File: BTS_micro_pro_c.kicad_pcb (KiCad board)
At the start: 2 copper layers, 33 x 17.8 mm, 5 parts, among them J1 FTDI, J2 I2C, J3 Analog, J6 Analog, J7 Digital

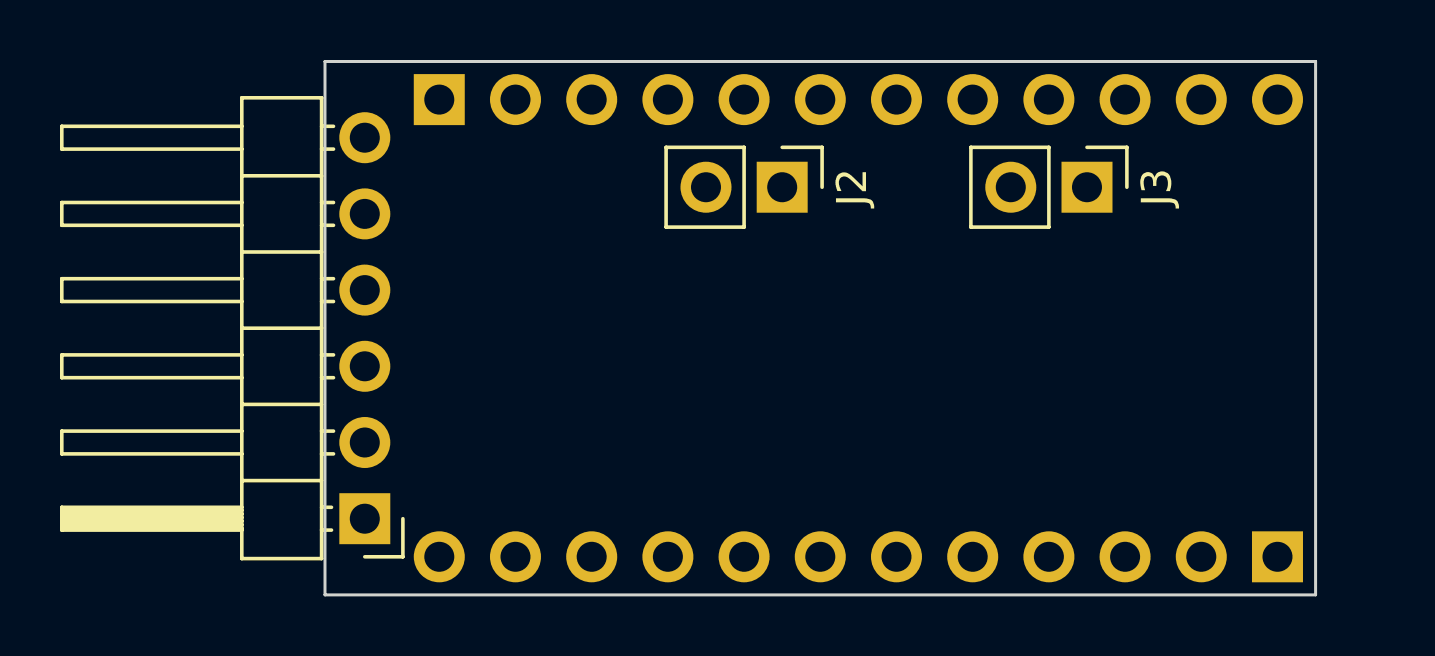
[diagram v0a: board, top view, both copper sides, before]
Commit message: Schematic potentially done, needs footprints assigned though.
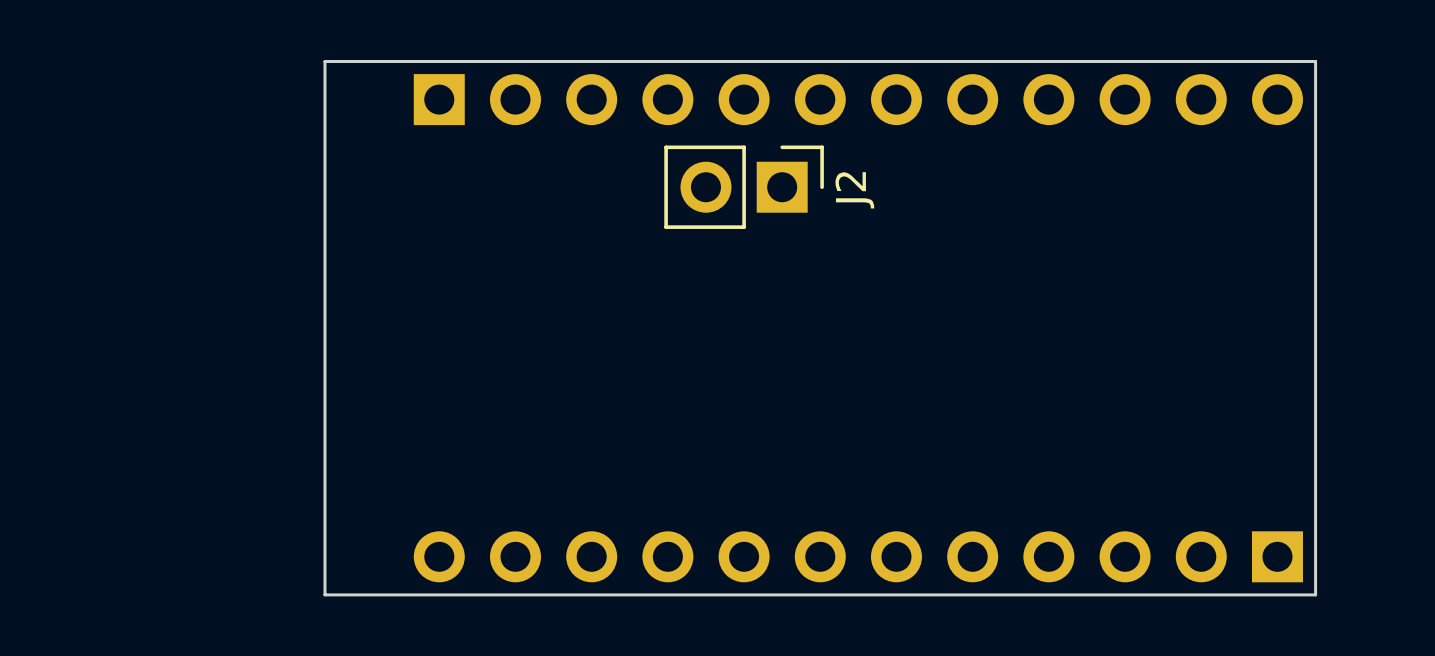
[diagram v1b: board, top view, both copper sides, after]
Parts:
- removed J1: FTDI, Connector_PinHeader_2.54mm:PinHeader_1x06_P2.54mm_Horizontal
- removed J3: Analog, Connector_PinHeader_2.54mm:PinHeader_1x02_P2.54mm_Vertical

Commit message: Finish rev1.
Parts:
- removed J2: I2C, Connector_PinHeader_2.54mm:PinHeader_1x02_P2.54mm_Vertical
- added C1: 10uF, Capacitor_SMD:C_0402_1005Metric, F.Cu at (114.1, 88.0)
- added C2: 22uF, Capacitor_SMD:C_0402_1005Metric, F.Cu at (114.9, 90.1)
- added C3: 22pF, Capacitor_SMD:C_0402_1005Metric, F.Cu at (128.8, 93.0)
- added C4: 22pF, Capacitor_SMD:C_0402_1005Metric, F.Cu at (128.9, 96.0)
- added C5: 1uF, Capacitor_SMD:C_0402_1005Metric, F.Cu at (116.5, 95.0)
- added C6: 0.1uF, Capacitor_SMD:C_0402_1005Metric, F.Cu at (116.1, 89.0)
- added C7: 1uF, Capacitor_SMD:C_0402_1005Metric, F.Cu at (114.1, 87.0)
- added C8: 0.1uF, Capacitor_SMD:C_0402_1005Metric, F.Cu at (114.1, 86.1)
- added D1: LED, LED_SMD:LED_0402_1005Metric, F.Cu at (130.7, 86.2)
- added D2: D, Diode_SMD:D_0402_1005Metric, F.Cu at (113.0, 90.9)
- added F1: 500mA Polyfuse, Fuse:Fuse_0805_2012Metric, F.Cu at (111.2, 91.1)
- added J1: USB4105-GF-A, USB4105-GF-A:GCT_USB4105-GF-A, F.Cu at (102.9, 91.1)
- added R1: 330, Resistor_SMD:R_0402_1005Metric, F.Cu at (128.8, 86.2)
- added R2: 1M, Resistor_SMD:R_0402_1005Metric, F.Cu at (128.4, 94.5)
- added R3: 10K, Resistor_SMD:R_0402_1005Metric, F.Cu at (123.4, 96.4)
- added R6: 5.1k, Resistor_SMD:R_0402_1005Metric, F.Cu at (109.0, 89.4)
- added R7: 5.1k, Resistor_SMD:R_0402_1005Metric, F.Cu at (109.0, 93.7)
- added R8: 10k, Resistor_SMD:R_0402_1005Metric, F.Cu at (122.9, 85.3)
- added U1: ATmega32U4-A, Package_DFN_QFN:QFN-44-1EP_7x7mm_P0.5mm_EP5.2x5.2mm, F.Cu at (121.2, 91.2)
- added U3: AMS1117-3.3, Package_TO_SOT_SMD:SOT-23-3, F.Cu at (111.2, 87.3)
- added Y1: 8Mhz Crystal, Crystal:Crystal_SMD_3225-4Pin_3.2x2.5mm, F.Cu at (131.1, 93.8)
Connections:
- net /~{RESET} renamed ~{RESET}
- J6 pad 1: VDC -> UVCC
- J6 pad 10: /MISO/D12 -> MISO/D12
- J6 pad 11: /MOSI/*D11 -> MOSI/*D11
- J6 pad 12: /SS/*D10 -> SS/*D10
- J6 pad 5: /A3 -> A3
- J6 pad 6: /A2 -> A2
- J6 pad 7: /A1 -> A1
- J6 pad 8: /A0 -> A0
- J6 pad 9: /SCK/D13 -> SCK/D13
- J7 pad 1: /*D9 -> *D9
- J7 pad 11: /RX -> RX
- J7 pad 12: /TX -> TX
- J7 pad 2: /D8 -> D8
- J7 pad 3: /D7 -> D7
- J7 pad 4: /*D6 -> *D6
- J7 pad 5: /*D5 -> *D5
- J7 pad 6: /D4 -> D4
- J7 pad 7: /*D3 -> *D3
- J7 pad 8: /D2 -> D2
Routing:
- net UVCC: track 0.00 -> 46.0 mm, vias 0 -> 3
- net GND: track 0.00 -> 45.1 mm, vias 0 -> 9
- net ~{RESET}: track 0.00 -> 37.1 mm, vias 0 -> 2
- net TX: track 0.00 -> 33.2 mm, vias 0 -> 1
- net D4: track 0.00 -> 26.4 mm, vias 0 -> 2
- net *D5: track 0.00 -> 26.2 mm, vias 0 -> 1
- net RX: track 0.00 -> 25.4 mm, vias 0 -> 1
- net VCC: track 0.00 -> 25.3 mm, vias 0 -> 6
- net *D9: track 0.00 -> 22.8 mm, vias 0 -> 1
- net MOSI/*D11: track 0.00 -> 18.5 mm, vias 0 -> 2
- net D8: track 0.00 -> 18.0 mm, vias 0 -> 1
- net MISO/D12: track 0.00 -> 17.8 mm, vias 0 -> 2
- net D7: track 0.00 -> 17.5 mm, vias 0 -> 1
- net SCK/D13: track 0.00 -> 16.8 mm, vias 0 -> 2
- net D2: track 0.00 -> 16.7 mm, vias 0 -> 1
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- added copper zone on B.Cu, net GND
- added copper zone on F.Cu, net GND
- added copper zone on In2.Cu, net VCC
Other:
- copper layers 2 -> 4

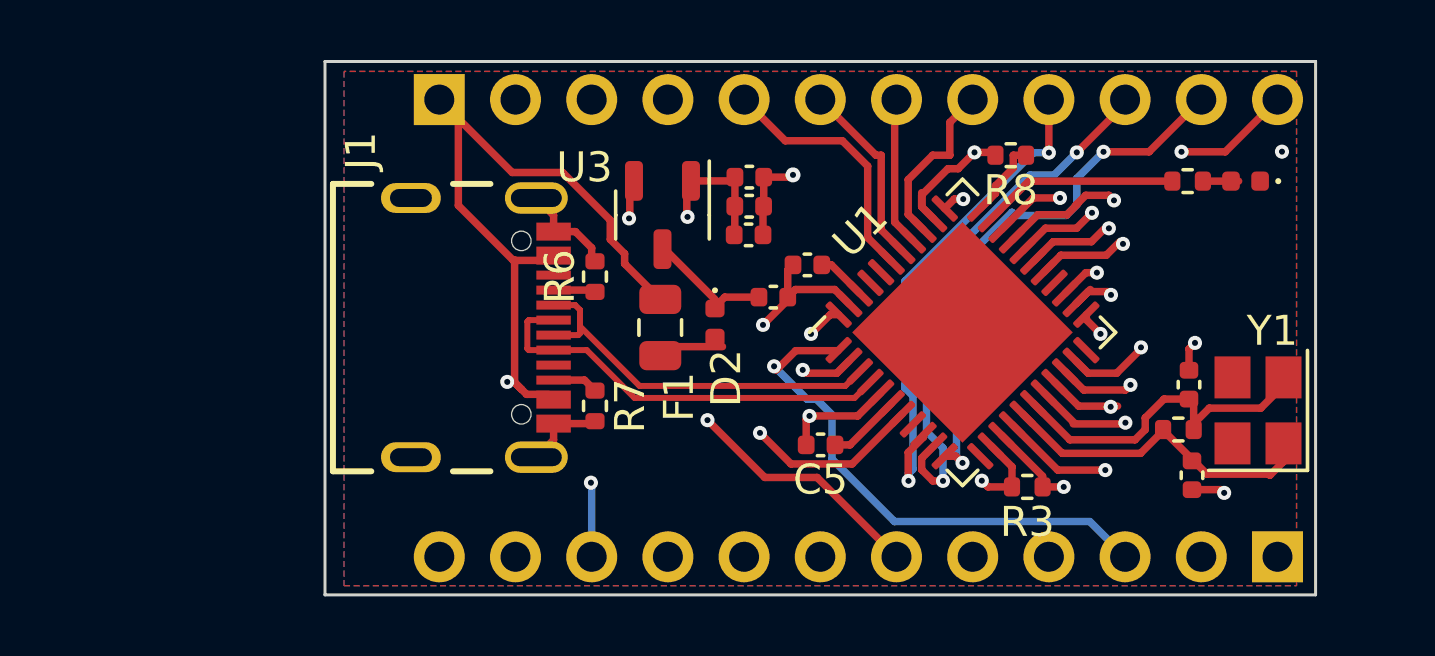
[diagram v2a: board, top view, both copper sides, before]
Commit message: Update project to rev 2.
This includes new I2C connector (STEMMA QT), fixed missing resistors on USB, change to easier to route osc.

Also includes custominng some footprints for space concerns.
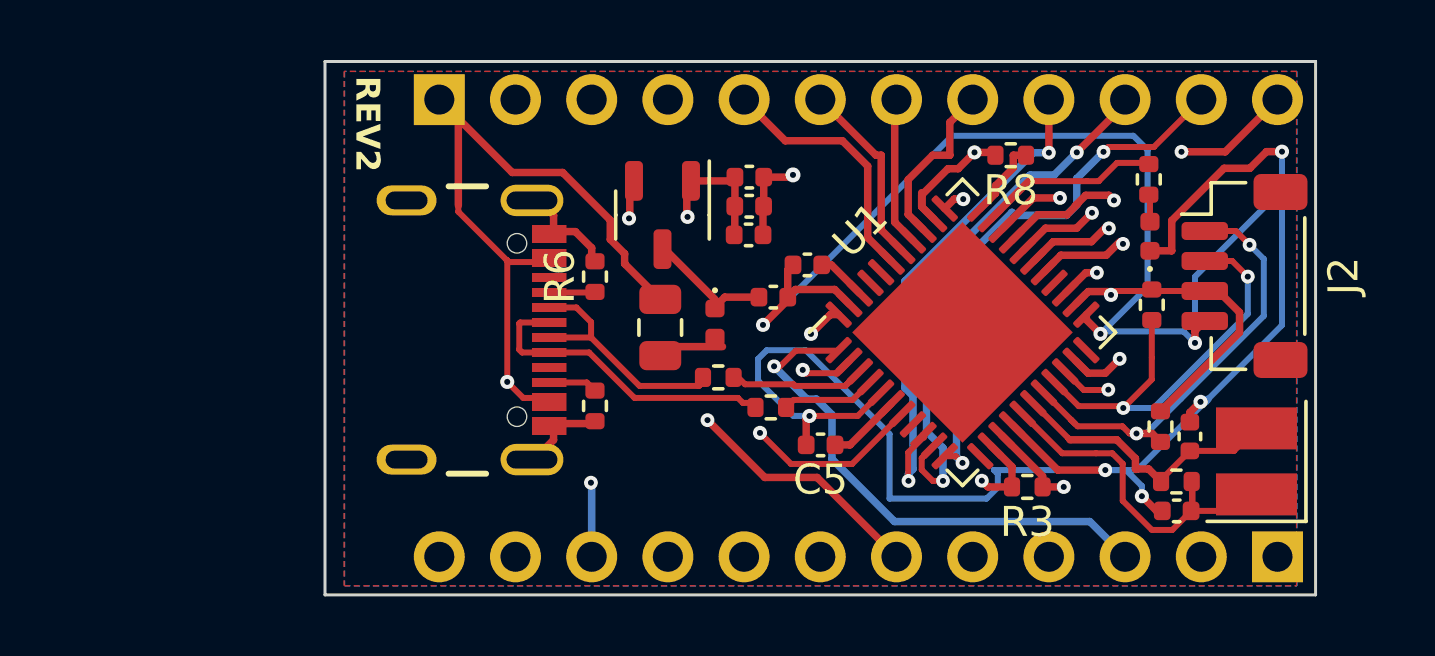
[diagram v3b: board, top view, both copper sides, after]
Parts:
- added J2: Conn_01x04, Connector_JST:JST_SH_BM04B-SRSS-TB_1x04-1MP_P1.00mm_Vertical, F.Cu at (130.7, 89.4)
- added R10: 10k, Resistor_SMD:R_0402_1005Metric, F.Cu at (127.6, 90.3)
- added R4: 22, Resistor_SMD:R_0402_1005Metric, F.Cu at (114.9, 93.8)
- added R5: 10k, Resistor_SMD:R_0402_1005Metric, F.Cu at (127.8, 94.4)
- added R9: 22, Resistor_SMD:R_0402_1005Metric, F.Cu at (113.1, 92.8)
- J1: footprint USB4105-GF-A:GCT_USB4105-GF-A -> Library:GCT_USB4105-GF-A
- J6, J7: footprint Connector_PinHeader_2.54mm:PinHeader_1x12_P2.54mm_Vertical -> Library:PinHeader_1x12_P2.54mm_Vertical
- Y1: footprint Crystal:Crystal_SMD_3225-4Pin_3.2x2.5mm -> Library:Crystal_SMD_3225-2Pin_3.2x2.5mm
- moved D1 3.68 mm to (127.5, 88.0), turned to 90 degrees
- moved R2 1.73 mm to (128.4, 96.2), turned to 180 degrees
- moved C3 1.73 mm to (128.8, 94.7)
- moved Y1 1.70 mm to (131.1, 95.5)
- moved R1 1.30 mm to (127.5, 86.2), turned to -90 degrees
- moved C4 1.29 mm to (128.4, 97.2), turned to 180 degrees
- moved J1 0.17 mm to (102.7, 91.2)
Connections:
- net Net-(U1-PC7) renamed /D13
- U1 pad 3: D- -> Net-(U1-D-)
- U1 pad 4: D+ -> Net-(U1-D+)
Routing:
- net GND: track 45.1 -> 119.9 mm, vias 9 -> 10
- net D2: track 16.7 -> 29.4 mm, vias 1 -> 2
- net *D3: track 15.8 -> 27.8 mm, vias 1 -> 2
- net VCC: track 25.3 -> 33.8 mm
- net Net-(U1-D-): track 0.00 -> 5.08 mm
- net D-: track 13.0 -> 8.01 mm
- net D+: track 14.1 -> 10.7 mm
- net Net-(U1-D+): track 0.00 -> 3.16 mm
- net /XTAL2: track 11.0 -> 12.7 mm
- net /XTAL1: track 11.0 -> 9.51 mm
- net RX: track 25.4 -> 23.9 mm
- net D4: track 26.4 -> 27.7 mm
- net TX: track 33.2 -> 34.6 mm
- net /D13: track 6.57 -> 6.06 mm
- added copper zone on In1.Cu, net GND
- added copper zone on B.Cu, net VCC
- removed copper zone on B.Cu, net GND
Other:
- board text added: "A0"
- board text added: "A1"
- board text added: "A2"
- board text added: "A3"
- board text added: "Boyd Technical Solutions, LLC Pro Micro C 2023"
- board text added: "D2"
- board text added: "D3"
- board text added: "D4"
- board text added: "D5"
- board text added: "D6"
- board text added: "D7"
- board text added: "D8"
- board text added: "D9"
- board text added: "GND"
- board text added: "MISO"
- board text added: "MOSI"
- board text added: "REV2"
- board text added: "RX"
- board text added: "SCK"
- board text added: "SS"
- board text added: "TX"
- board text added: "UVCC"
- board text added: "VCC"
- board text added: "~{RESET}"
